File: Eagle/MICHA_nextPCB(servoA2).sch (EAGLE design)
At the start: 71 parts, among them IC1 LM4041A12LP, K1 PIN20X2, T1 BSS84, U1 ARDUINO_MKR_ZERO, U2 MIKROE_CLICK_UPGRADE, U3 MAX4528CSA, X1 SS-7188S-A-NF_V2, X2 SS-7188S-A-NF_V2, X3 SS-7188S-A-NF_V2, X4 SS-7188S-A-NF_V2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

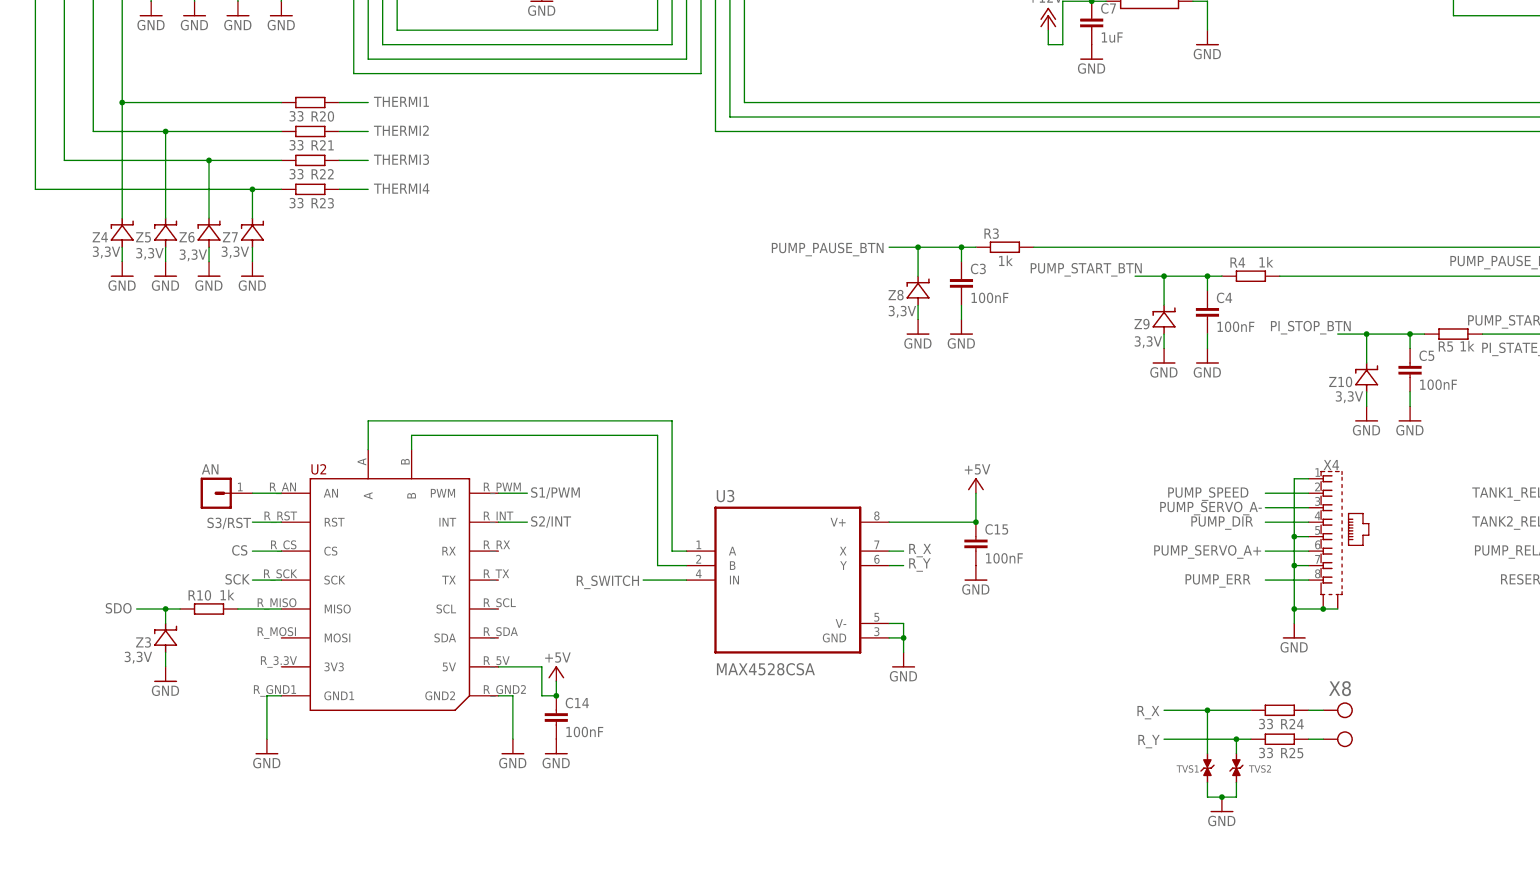
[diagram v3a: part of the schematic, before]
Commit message: Btn & thermis zener replaced by Schottky
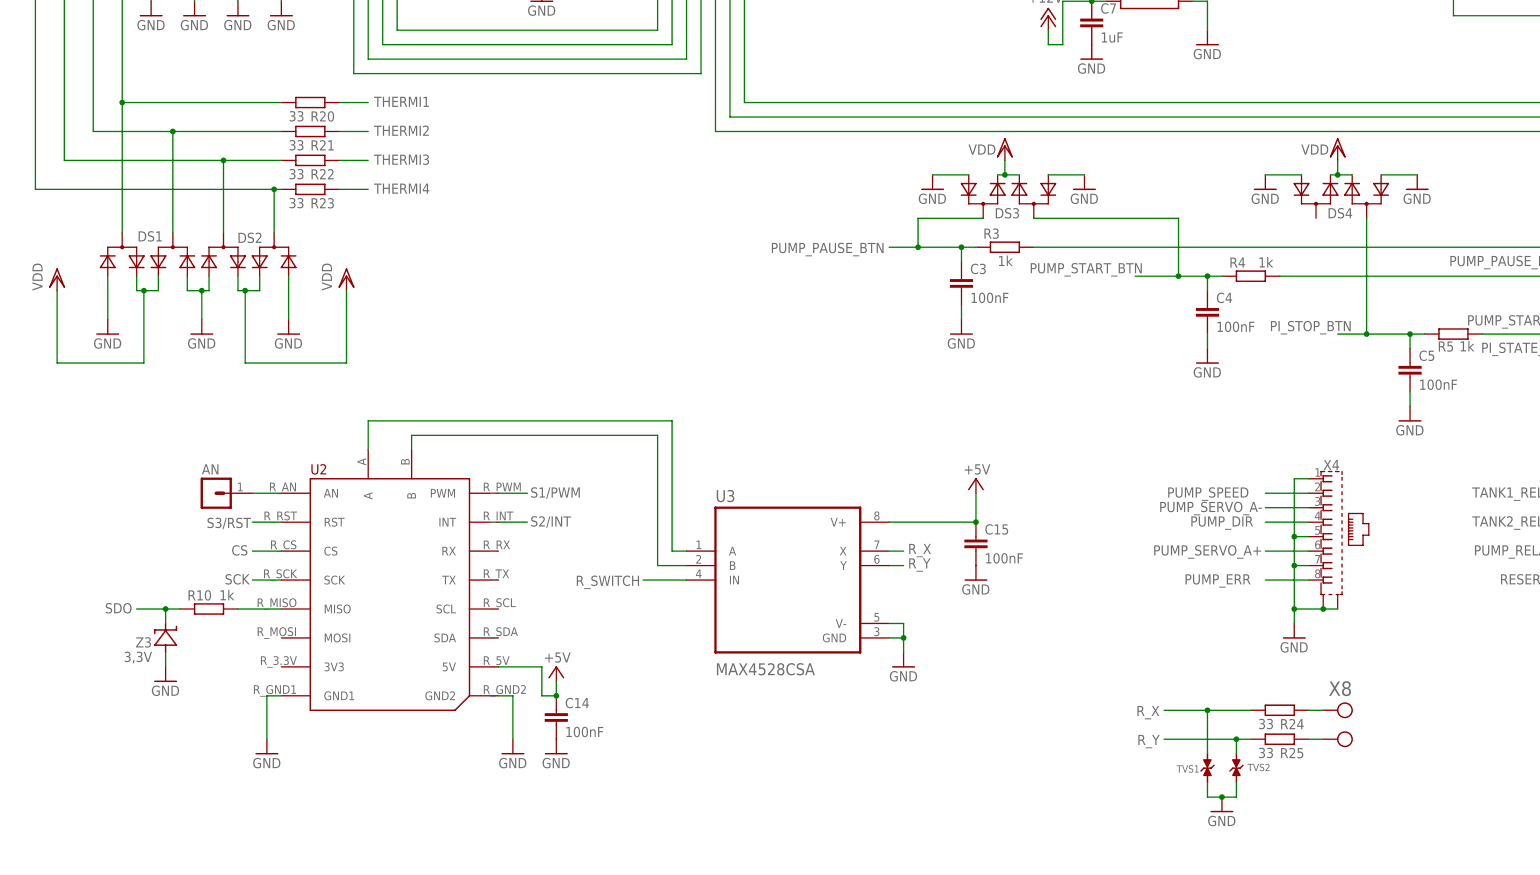
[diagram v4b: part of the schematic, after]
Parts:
- removed Z10, Z4, Z5, Z6, Z7, Z8, Z9: 3,3V, Zener_SMA:ZENER_SMA
- added DS1, DS2, DS3, DS4: SDM10M45SD, SchottkyDiodes_SDM10M45SD:SDM10M45SD
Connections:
- net GND: now also DS1.A2, DS1.A3, DS2.A2, DS2.A3, DS3.A2, DS3.A3, DS4.A2, DS4.A3; no longer Z10.A, Z4.A, Z5.A, Z6.A, Z7.A, Z8.A, Z9.A
- net N$11: now also DS1.C1; no longer Z4.C
- net N$12: now also DS1.C; no longer Z5.C
- net N$13: now also DS2.C1; no longer Z6.C
- net N$14: now also DS2.C; no longer Z7.C
- net PI_STOP_BTN: now also DS4.C1; no longer Z10.C
- net PUMP_PAUSE_BTN: now also DS3.C; no longer Z8.C
- net PUMP_START_BTN: now also DS3.C1; no longer Z9.C
- net VDD: now also DS1.A1, DS1.A4, DS2.A1, DS2.A4, DS3.A1, DS3.A4, DS4.A1, DS4.A4

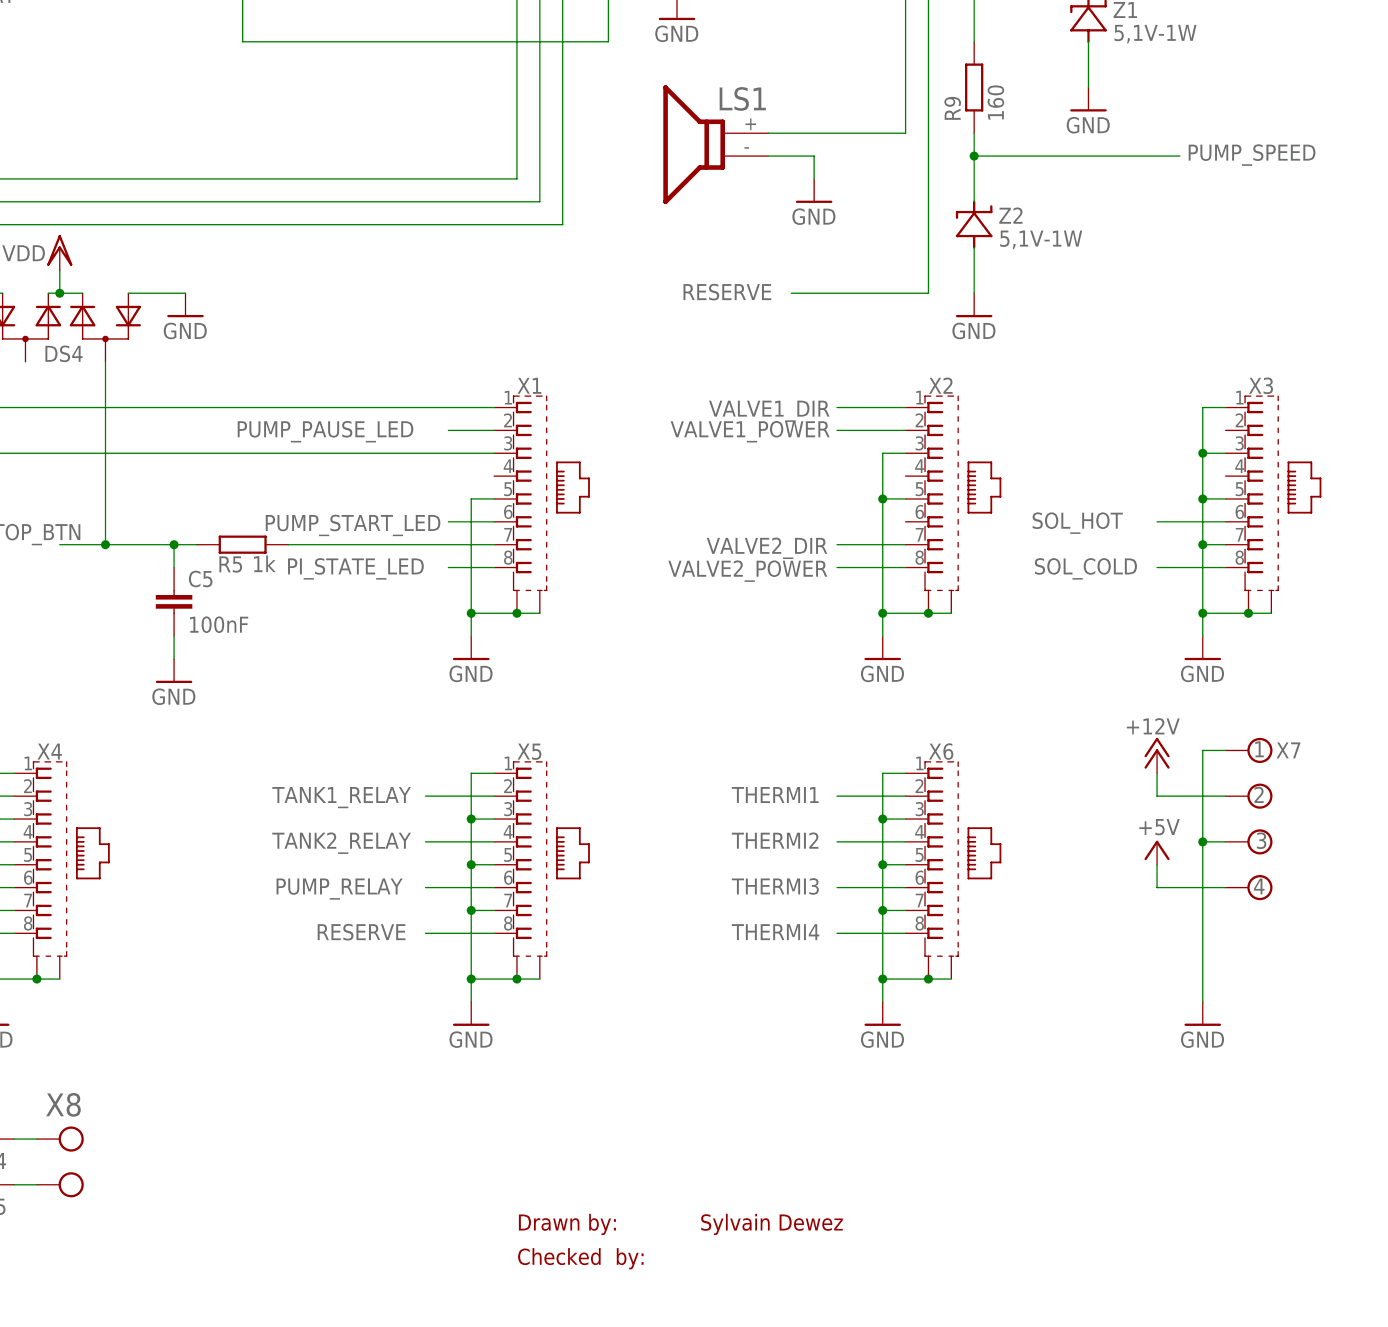
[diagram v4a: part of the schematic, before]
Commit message: add jumpers for reserve and pump_relay
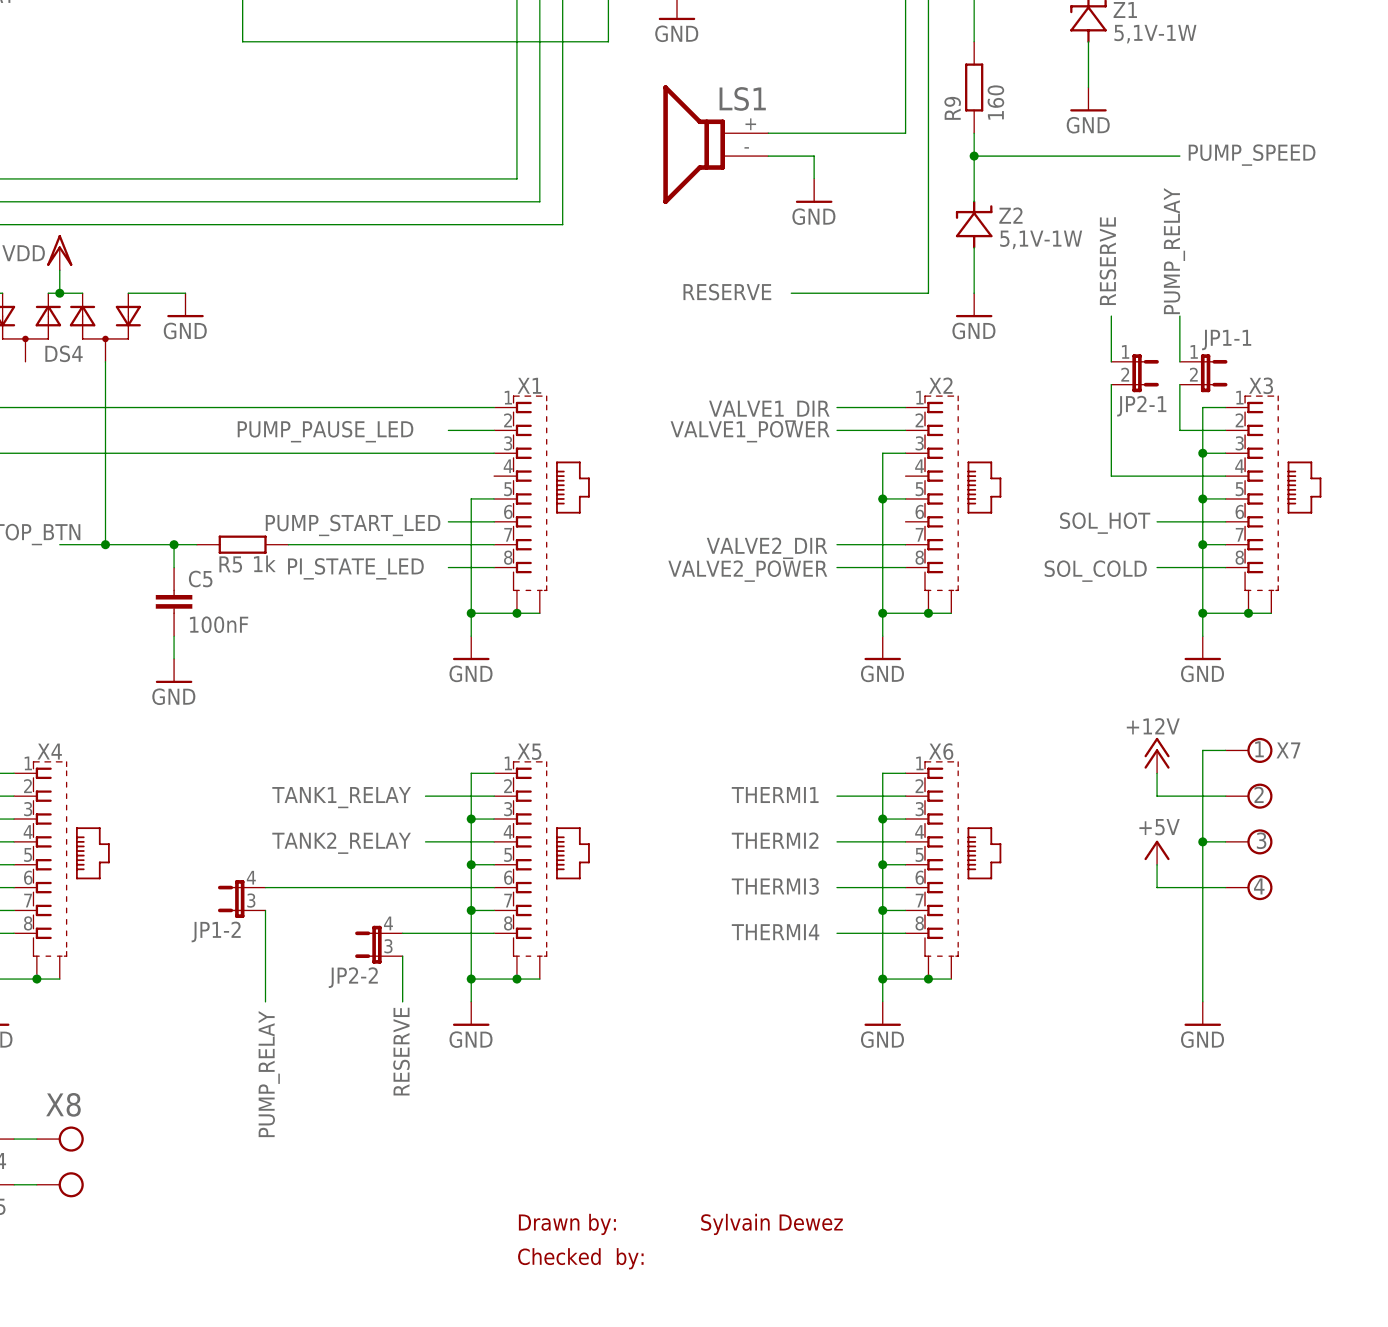
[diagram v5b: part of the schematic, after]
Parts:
- added JP1, JP2: (no value), jumper:JP2QE
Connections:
- new net N$19: JP1-2.2, X5.6
- new net N$20: JP1-1.2, X3.2
- new net N$21: JP2-2.2, X5.8
- new net N$22: JP2-1.2, X3.4
- net PUMP_RELAY: now also JP1-1.1, JP1-2.1; no longer X5.6
- net RESERVE: now also JP2-1.1, JP2-2.1; no longer X5.8
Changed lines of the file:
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@@
 <part name="DS4" library="SchottkyDiodes_SDM10M45SD" deviceset="SDM10M45SD" device=""/>
 <part name="VDD6" library="supply1" library_urn="urn:adsk.eagle:library:371" deviceset="VDD" device=""/>
+<part name="JP1" library="jumper" library_urn="urn:adsk.eagle:library:252" deviceset="JP2QE" device="" package3d_urn="urn:adsk.eagle:package:15450/1"/>
+<part name="JP2" library="jumper" library_urn="urn:adsk.eagle:library:252" deviceset="JP2QE" device="" package3d_urn="urn:adsk.eagle:package:15450/1"/>
 </parts>
 <sheets>
@@
 <instance part="VDD6" gate="G$1" x="238.76" y="129.54" smashed="yes">
 <attribute name="VALUE" x="237.236" y="129.794" size="1.778" layer="96" rot="R180"/>
+</instance>
+<instance part="JP1" gate="-1" x="365.76" y="116.84" smashed="yes" rot="R270">
+<attribute name="NAME" x="371.348" y="120.396" size="1.778" layer="95" rot="R180"/>
+<attribute name="VALUE" x="365.76" y="111.125" size="1.778" layer="96"/>
+</instance>
+<instance part="JP1" gate="-2" x="259.08" y="55.88" smashed="yes" rot="R90">
+<attribute name="NAME" x="259.08" y="54.61" size="1.778" layer="95" rot="R180"/>
+<attribute name="VALUE" x="259.08" y="61.595" size="1.778" layer="96" rot="R180"/>
+</instance>
+<instance part="JP2" gate="-1" x="358.14" y="116.84" smashed="yes" rot="R270">
+<attribute name="NAME" x="356.362" y="111.252" size="1.778" layer="95"/>
+<attribute name="VALUE" x="358.14" y="111.125" size="1.778" layer="96"/>
+</instance>
+<instance part="JP2" gate="-2" x="274.32" y="50.8" smashed="yes" rot="R90">
+<attribute name="NAME" x="274.32" y="49.53" size="1.778" layer="95" rot="R180"/>
+<attribute name="VALUE" x="274.32" y="56.515" size="1.778" layer="96" rot="R180"/>
 </instance>
 </instances>
@@
 <segment>
 <wire x1="368.3" y1="99.06" x2="360.68" y2="99.06" width="0.1524" layer="91"/>
-<label x="346.71" y="98.298" size="1.778" layer="95"/>
+<label x="359.918" y="100.076" size="1.778" layer="95" rot="R180"/>
 <pinref part="X3" gate="G$1" pin="6"/>
 </segment>
@@
 <pinref part="X3" gate="G$1" pin="8"/>
 <wire x1="368.3" y1="93.98" x2="360.68" y2="93.98" width="0.1524" layer="91"/>
-<label x="346.964" y="93.218" size="1.778" layer="95"/>
+<label x="359.664" y="94.742" size="1.778" layer="95" rot="R180"/>
 </segment>
 <segment>
@@
 </segment>
 <segment>
-<wire x1="287.02" y1="58.42" x2="279.4" y2="58.42" width="0.1524" layer="91"/>
-<label x="262.636" y="57.658" size="1.778" layer="95"/>
-<pinref part="X5" gate="G$1" pin="6"/>
+<pinref part="JP1" gate="-2" pin="1"/>
+<wire x1="261.62" y1="55.88" x2="261.62" y2="45.72" width="0.1524" layer="91"/>
+<label x="260.858" y="44.704" size="1.778" layer="95" rot="R270"/>
+</segment>
+<segment>
+<pinref part="JP1" gate="-1" pin="1"/>
+<wire x1="363.22" y1="116.84" x2="363.22" y2="121.92" width="0.1524" layer="91"/>
+<label x="363.22" y="121.92" size="1.778" layer="95" rot="R90"/>
 </segment>
 </net>
@@
 </segment>
 <segment>
-<wire x1="287.02" y1="53.34" x2="279.4" y2="53.34" width="0.1524" layer="91"/>
-<label x="267.208" y="52.578" size="1.778" layer="95"/>
-<pinref part="X5" gate="G$1" pin="8"/>
+<pinref part="JP2" gate="-2" pin="1"/>
+<wire x1="276.86" y1="50.8" x2="276.86" y2="45.72" width="0.1524" layer="91"/>
+<label x="275.844" y="45.212" size="1.778" layer="95" rot="R270"/>
+</segment>
+<segment>
+<pinref part="JP2" gate="-1" pin="1"/>
+<wire x1="355.6" y1="116.84" x2="355.6" y2="121.92" width="0.1524" layer="91"/>
+<label x="356.108" y="122.936" size="1.778" layer="95" rot="R90"/>
 </segment>
 </net>
@@
 </segment>
 </net>
+<net name="N$19" class="0">
+<segment>
+<pinref part="X5" gate="G$1" pin="6"/>
+<pinref part="JP1" gate="-2" pin="2"/>
+<wire x1="287.02" y1="58.42" x2="261.62" y2="58.42" width="0.1524" layer="91"/>
+</segment>
+</net>
+<net name="N$20" class="0">
+<segment>
+<pinref part="X3" gate="G$1" pin="2"/>
+<wire x1="368.3" y1="109.22" x2="363.22" y2="109.22" width="0.1524" layer="91"/>
+<pinref part="JP1" gate="-1" pin="2"/>
+<wire x1="363.22" y1="109.22" x2="363.22" y2="114.3" width="0.1524" layer="91"/>
+</segment>
+</net>
+<net name="N$21" class="0">
+<segment>
+<pinref part="X5" gate="G$1" pin="8"/>
+<pinref part="JP2" gate="-2" pin="2"/>
+<wire x1="287.02" y1="53.34" x2="276.86" y2="53.34" width="0.1524" layer="91"/>
+</segment>
+</net>
+<net name="N$22" class="0">
+<segment>
+<pinref part="X3" gate="G$1" pin="4"/>
+<pinref part="JP2" gate="-1" pin="2"/>
+<wire x1="368.3" y1="104.14" x2="355.6" y2="104.14" width="0.1524" layer="91"/>
+<wire x1="355.6" y1="104.14" x2="355.6" y2="114.3" width="0.1524" layer="91"/>
+</segment>
+</net>
